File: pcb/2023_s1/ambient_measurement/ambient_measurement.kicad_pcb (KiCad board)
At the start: 2 copper layers, 12 parts, among them J1 Screw_Terminal_01x03, J2 Screw_Terminal_01x04, U1 NRF24L01_Breakout

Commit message: update, repositioned through holes
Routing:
- net D12: track 76.3 -> 82.9 mm
- net D14: track 84.6 -> 89.8 mm
- net D27: track 106.9 -> 108.3 mm

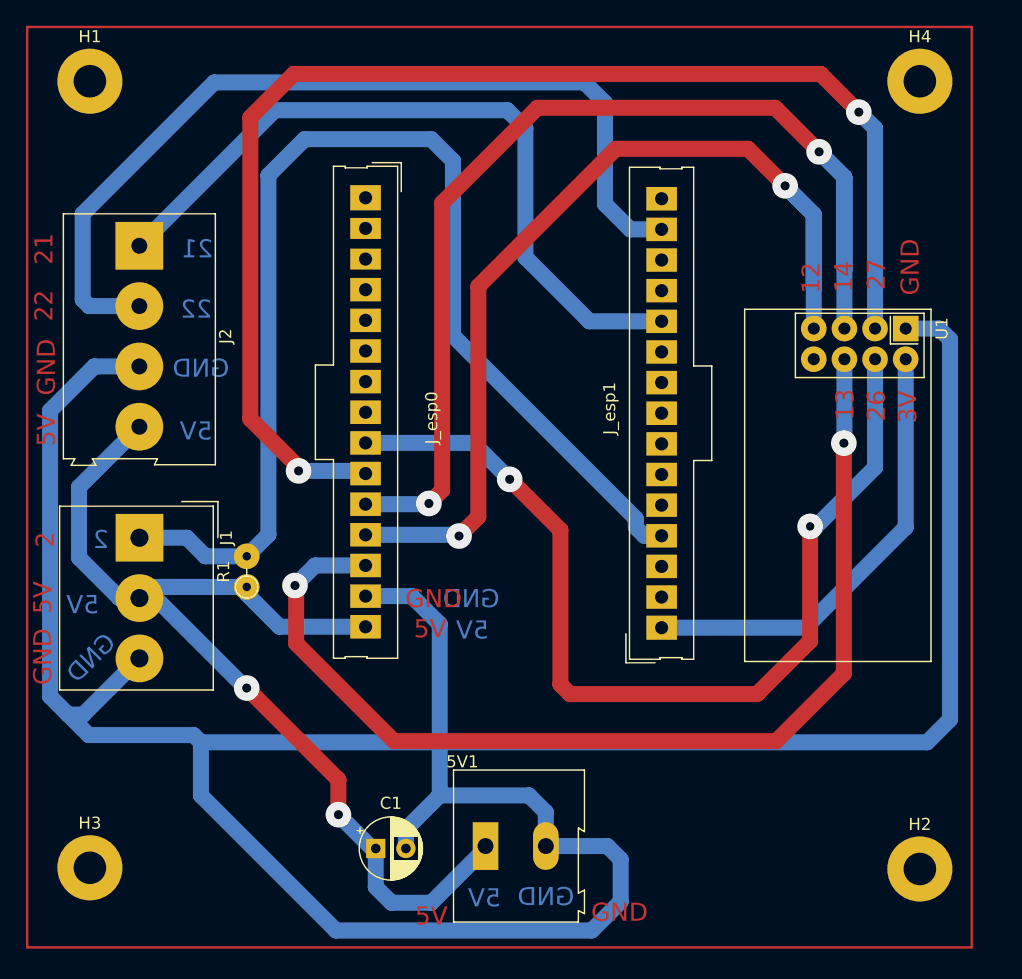
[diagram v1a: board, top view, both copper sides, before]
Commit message: update, changed the dht22 pin from 2 to 25, added a ceramic capacitor, and rerouted some elements
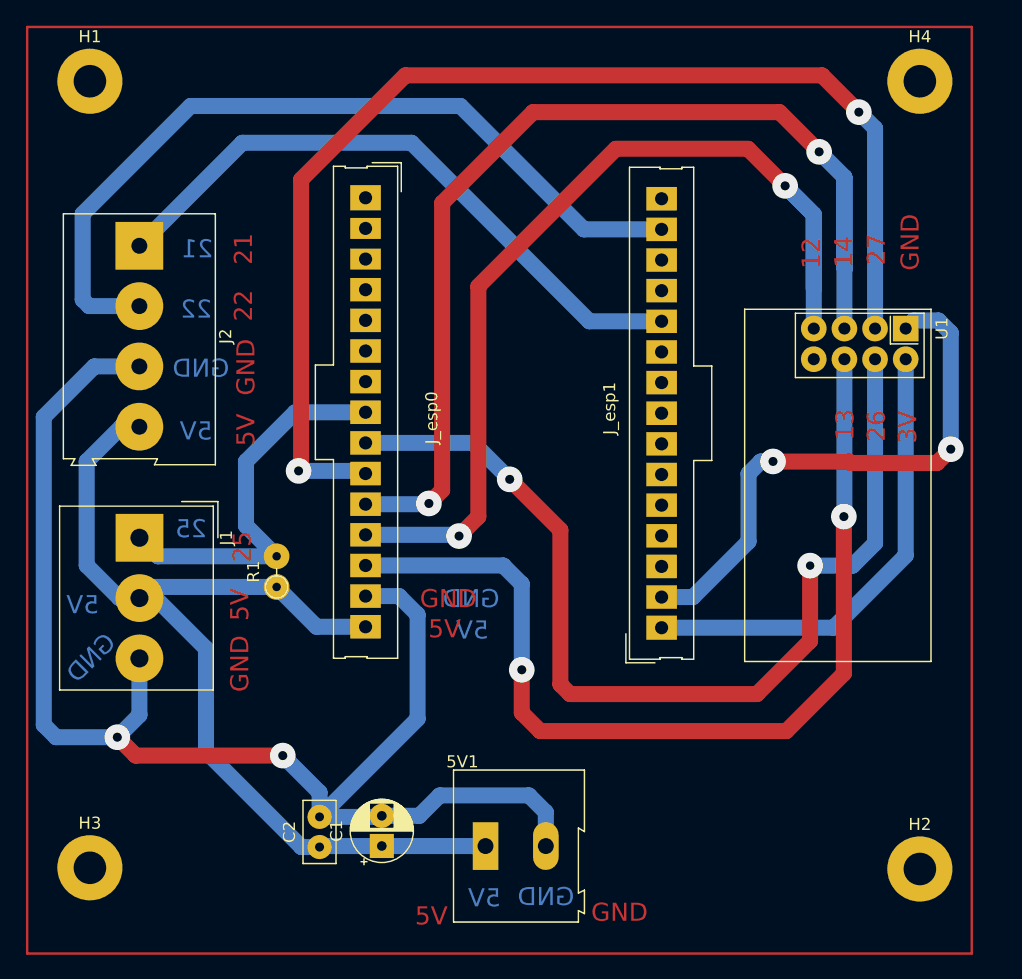
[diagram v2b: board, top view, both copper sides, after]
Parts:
- added C2: C_Generic, Capacitor_THT:C_Disc_D5.0mm_W2.5mm_P2.50mm, F.Cu at (199.1, 121.9)
- R1: value 4.7k -> 10k
- moved R1 2.48 mm to (195.6, 100.3)
- moved C1 0.54 mm to (204.3, 121.8), turned to 90 degrees
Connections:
- J1 pad 1: D2 -> D25
- R1 pad 2: D2 -> D25
- U1 pad 1: GND5V -> GND2
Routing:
- net GND5V: track 247.0 -> 117.7 mm, vias 0 -> 2
- net D2: track 98.2 -> 0.00 mm
- net GND2: track 0.00 -> 46.5 mm, vias 0 -> 2
- net D25: track 0.00 -> 32.5 mm
- net D13: track 88.5 -> 79.6 mm
- net D27: track 108.3 -> 99.4 mm
- net D21: track 61.5 -> 53.0 mm
- net D22: track 74.5 -> 68.0 mm
- net 5v: track 84.9 -> 82.6 mm, vias 2 -> 0
- net D26: track 80.7 -> 82.5 mm
- net 3V3: track 37.6 -> 39.0 mm
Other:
- board text added: "25"
- board text removed: "2"

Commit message: update, repositioned sensors and rf module so we can use shorter tracks and looks better
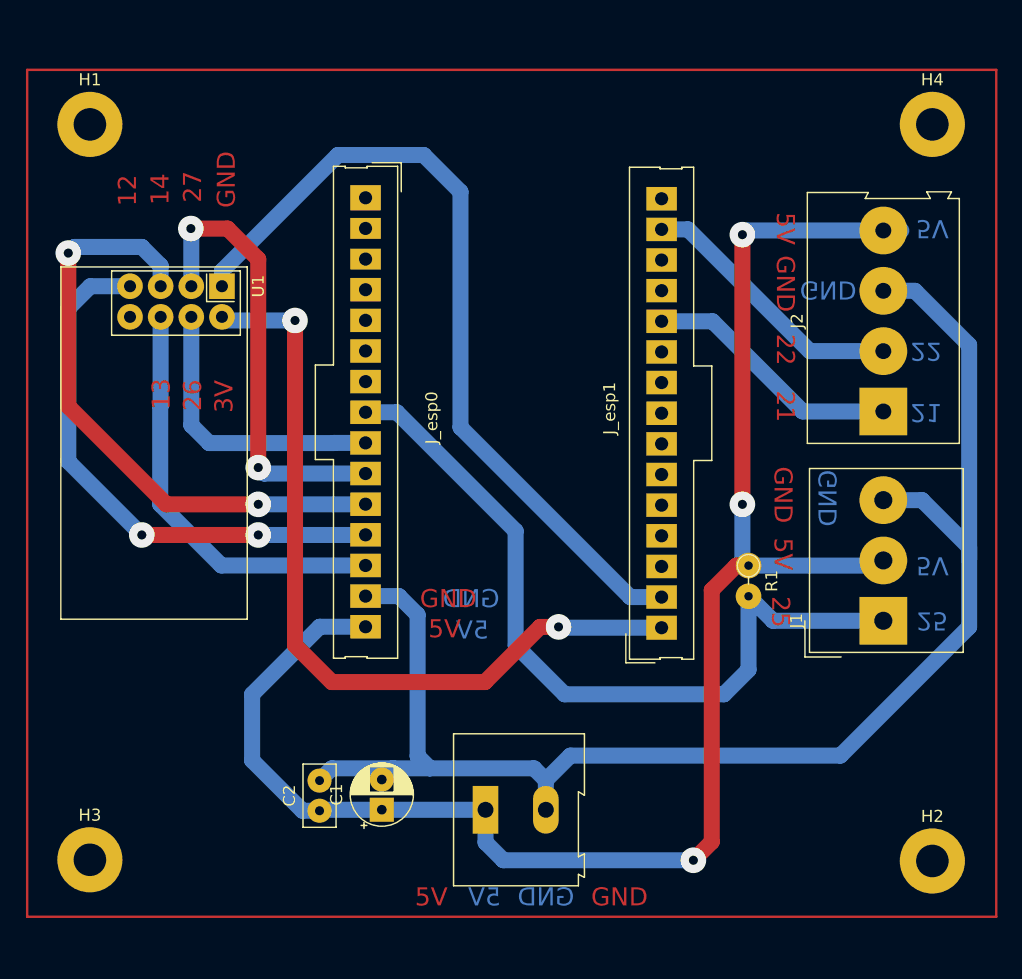
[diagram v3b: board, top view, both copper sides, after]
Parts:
- moved J2 63.2 mm to (245.9, 85.8), turned to 90 degrees
- moved J1 62.0 mm to (245.9, 103.1), turned to 90 degrees
- moved U1 56.8 mm to (191.0, 75.4)
- moved R1 39.2 mm to (234.7, 98.6), turned to -90 degrees
- moved H4 3.72 mm to (249.9, 62.0)
- moved H1 3.58 mm to (180.1, 62.0)
- moved 5V1 3.01 mm to (212.9, 118.8)
- moved C1 3.01 mm to (204.3, 118.8)
- moved C2 3.01 mm to (199.1, 118.9)
- moved H2 1.23 mm to (249.9, 123.0)
- moved H3 0.66 mm to (180.1, 122.9)
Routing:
- net D27: track 99.4 -> 38.1 mm
- net D26: track 82.5 -> 24.0 mm, vias 2 -> 0
- net 5v: track 82.6 -> 138.3 mm, vias 0 -> 3
- net D22: track 68.0 -> 22.6 mm
- net D13: track 79.6 -> 34.7 mm, vias 2 -> 0
- net D14: track 89.5 -> 50.9 mm
- net D12: track 82.9 -> 45.8 mm
- net D25: track 32.5 -> 65.9 mm
- net D21: track 53.0 -> 21.5 mm
- net 3V3: track 39.0 -> 66.7 mm, vias 0 -> 2
- net GND2: track 46.5 -> 68.3 mm, vias 2 -> 0
- net GND5V: track 117.7 -> 124.0 mm, vias 2 -> 0
